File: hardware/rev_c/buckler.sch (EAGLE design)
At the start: 61 parts, among them J1 DB25_5747846, J2 DM3AT-SF-PEJM5, J3 GROVE-CONNECTOR-DIP(4P-2.0), J4 GROVE-CONNECTOR-DIP(4P-2.0), J5 GROVE-CONNECTOR-DIP(4P-2.0), J6 GROVE-CONNECTOR-DIP(4P-2.0), J7 NRF52832DK_SHIELD, U1 ADXL327, U2 MAX44009, U3 MPU-9250, U4 MS5637-02BA03, U5 SI7021-A20-GM1, U6 SIP32510

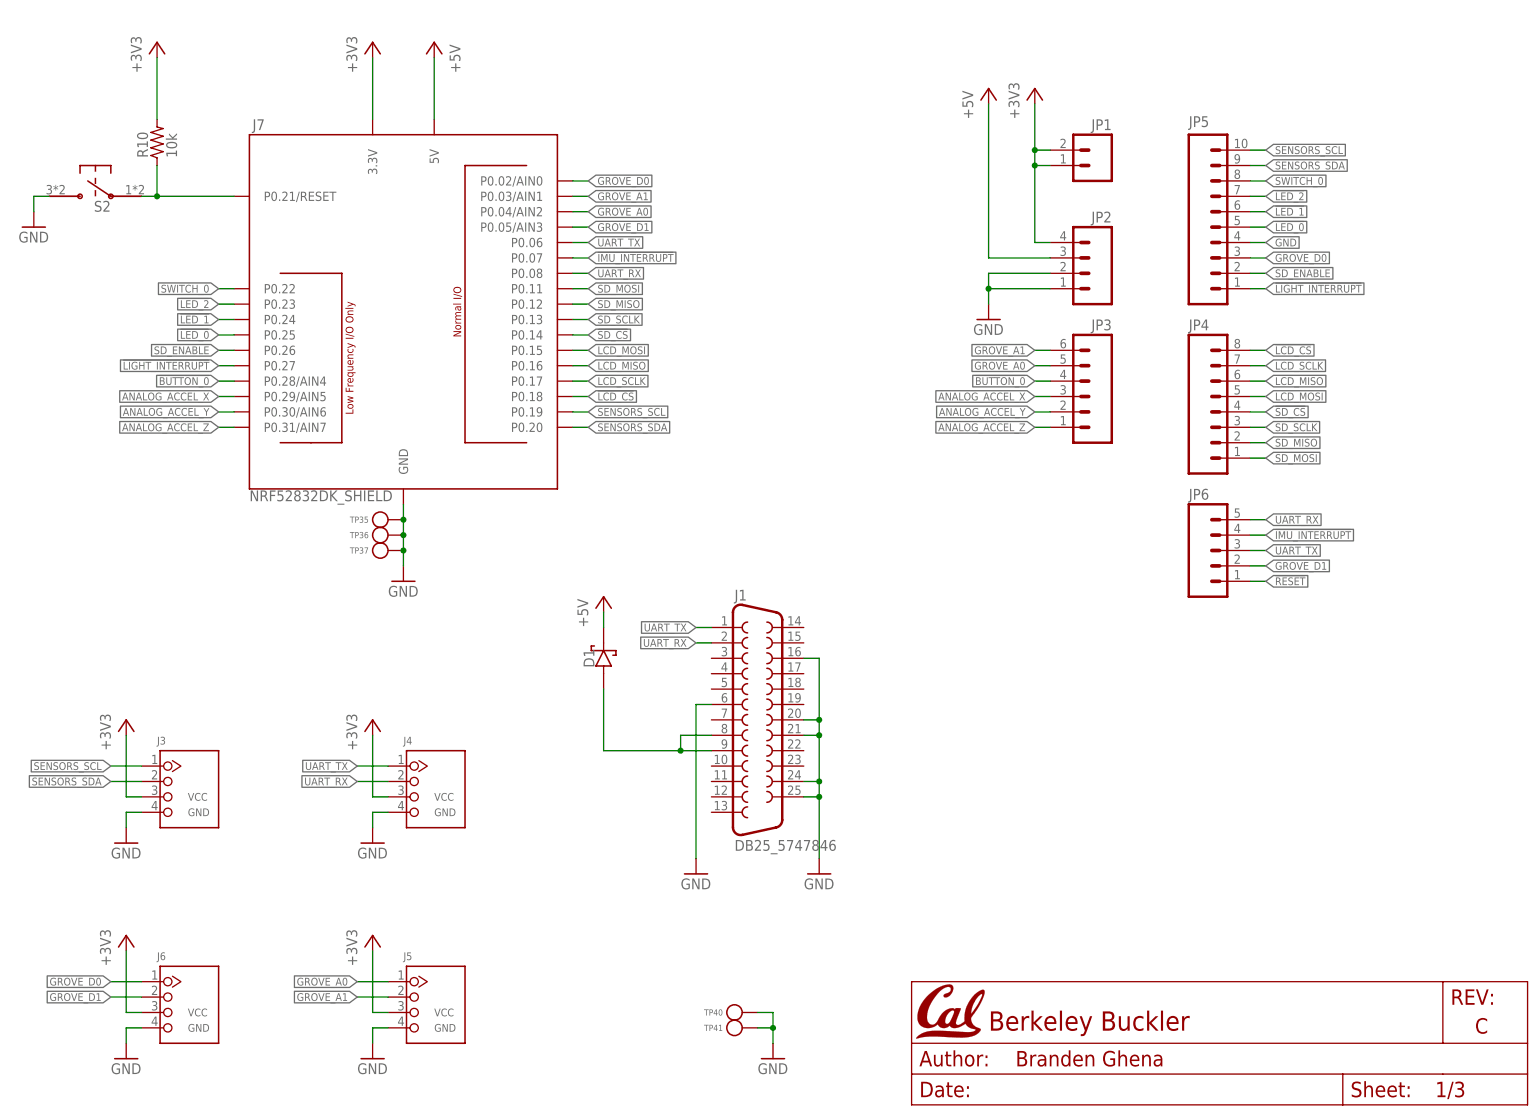
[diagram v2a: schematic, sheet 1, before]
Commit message: renumber headers
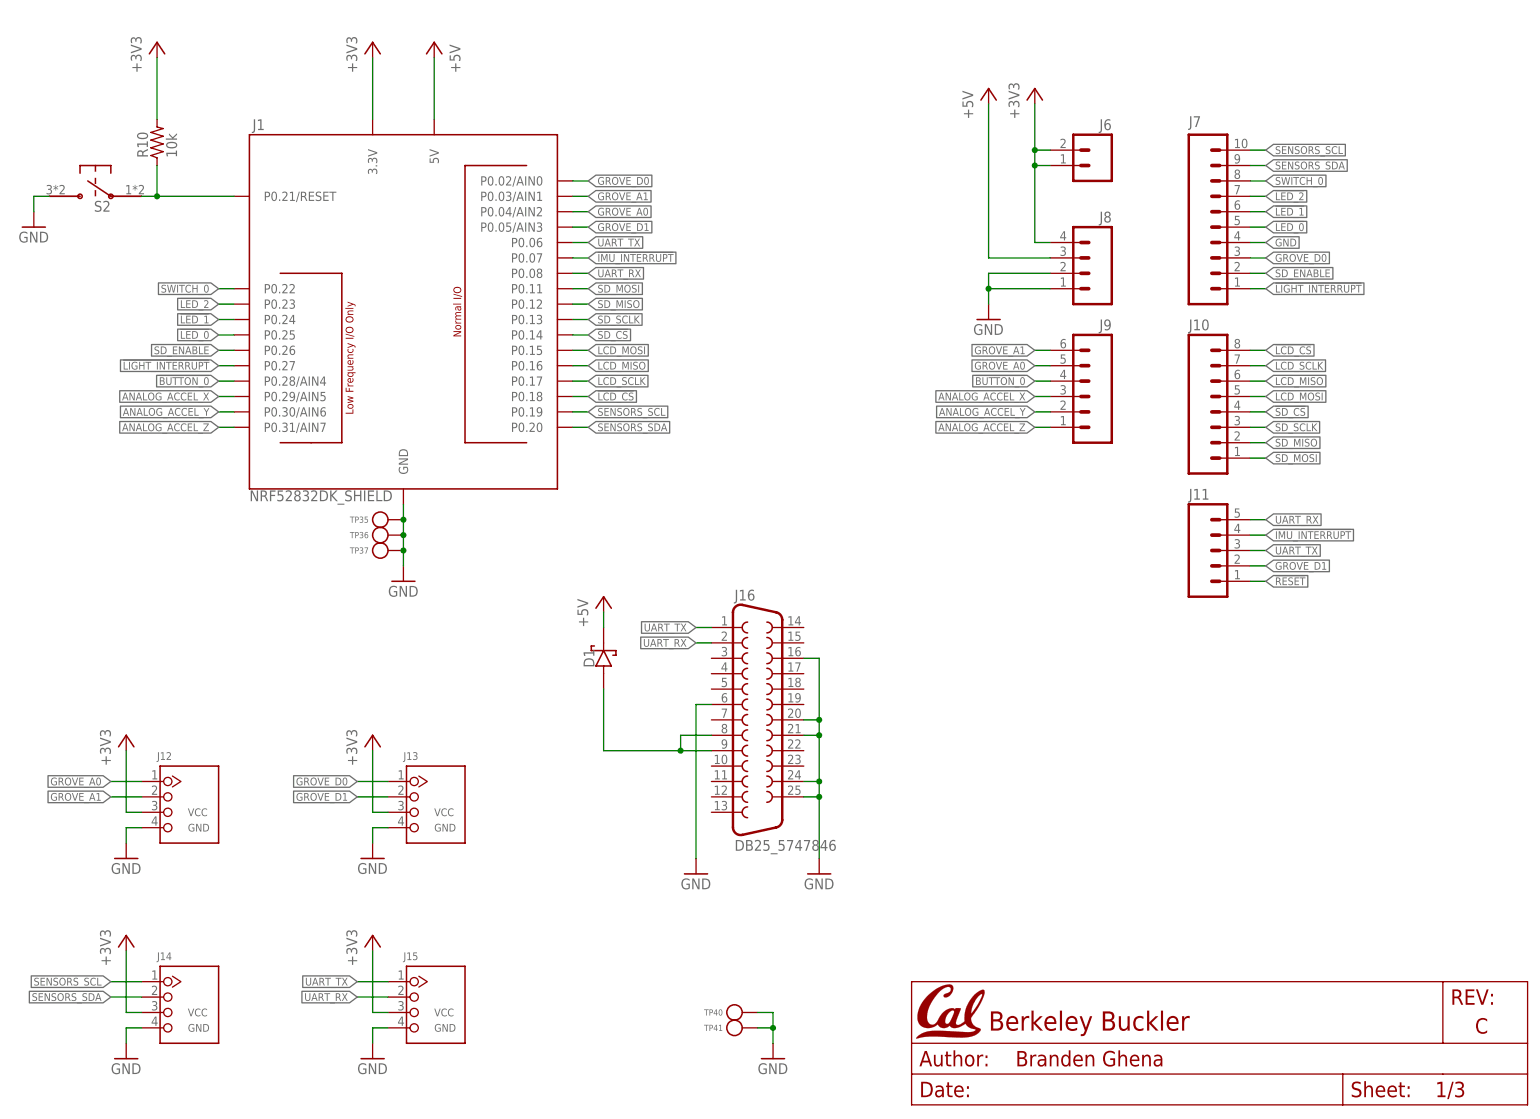
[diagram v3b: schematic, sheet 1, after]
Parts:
- removed J3, J4: GROVE-CONNECTOR-DIP(4P-2.0), headers:GROVE-CONNECTOR-DIP(4P-2.0)
- removed JP1: (no value), SparkFun-Connectors:M02PTH
- removed JP5: M10", SparkFun-Connectors:M10"
- added J12, J13, J14: GROVE-CONNECTOR-DIP(4P-2.0), headers:GROVE-CONNECTOR-DIP(4P-2.0)
- added J16: DB25_5747846, headers:DB25_5747846
- J1: value DB25_5747846 -> NRF52832DK_SHIELD; device headers:DB25_5747846 -> headers:NRF52832DK_SHIELD; DESCRIPTION CONN D-SUB RCPT 25POS R/A SOLDER -> (none); DIGIKEY1 (none) -> S1011EC-10-ND; DIGIKEY2 (none) -> S1011EC-08-ND; DIGIKEY3 (none) -> S1011EC-08-ND; DIGIKEY4 (none) -> S1011EC-06-ND; DIGIKEY5 (none) -> S1011EC-09-ND; MANUFACTURER TE Connectivity AMP Connectors -> (none); MPN 5747846-4 -> (none)
- J6: value GROVE-CONNECTOR-DIP(4P-2.0) -> (none); device headers:GROVE-CONNECTOR-DIP(4P-2.0) -> SparkFun-Connectors:M02PTH; DESCRIPTION Grove - Universal 4 pin connector -> (none); DIGIKEY (none) -> S1011EC-02-ND; MANUFACTURER Seeed Studio -> (none); MOUSER 713-110990030 -> (none); MPN 110990030 -> (none)
- J7: value NRF52832DK_SHIELD -> M10"; device headers:NRF52832DK_SHIELD -> SparkFun-Connectors:M10"; DIGIKEY (none) -> S1011EC-10-ND; DIGIKEY1 S1011EC-10-ND -> (none); DIGIKEY2 S1011EC-08-ND -> (none); DIGIKEY3 S1011EC-08-ND -> (none); DIGIKEY4 S1011EC-06-ND -> (none); DIGIKEY5 S1011EC-09-ND -> (none)
- renumbered J2 to J17, J5 to J15, JP2 to J8, JP3 to J9, JP4 to J10, JP6 to J11
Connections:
- net !BUTTON_0: now also J1.P0.28/AIN4; no longer J7.P0.28/AIN4
- net !IMU_INTERRUPT: now also J1.P0.07; no longer J7.P0.07
- net !LCD_CS: now also J1.P0.18; no longer J7.P0.18
- net !LED_0: now also J1.P0.25, J7.5; no longer J7.P0.25, JP5.5
- net !LED_1: now also J1.P0.24, J7.6; no longer J7.P0.24, JP5.6
- net !LED_2: now also J1.P0.23, J7.7; no longer J7.P0.23, JP5.7
- net !LIGHT_INTERRUPT: now also J1.P0.27, J7.1; no longer J7.P0.27, JP5.1
- net !RESET: now also J1.P0.21/RESET; no longer J7.P0.21/RESET
- net !SD_CS: now also J1.P0.14; no longer J7.P0.14
- net +3V3: now also J1.3.3V, J12.3, J13.3, J14.3, J6.1, J6.2; no longer J3.3, J4.3, J6.3, J7.3.3V, JP1.1, JP1.2
- net +5V: now also J1.5V; no longer J7.5V
- net 5V_IN: now also J16.8, J16.9; no longer J1.8, J1.9
- net ANALOG_ACCEL_X: now also J1.P0.29/AIN5; no longer J7.P0.29/AIN5
- net ANALOG_ACCEL_Y: now also J1.P0.30/AIN6; no longer J7.P0.30/AIN6
- net ANALOG_ACCEL_Z: now also J1.P0.31/AIN7; no longer J7.P0.31/AIN7
- net GND: now also J1.GND, J12.4, J13.4, J14.4, J16.16, J16.20, J16.21, J16.24, J16.25, J16.6, J7.4; no longer J1.16, J1.20, J1.21, J1.24, J1.25, J1.6, J3.4, J4.4, J6.4, J7.GND, JP5.4
- net GROVE_A0: now also J1.P0.04/AIN2, J12.1; no longer J15.1, J7.P0.04/AIN2
- net GROVE_A1: now also J1.P0.03/AIN1, J12.2; no longer J15.2, J7.P0.03/AIN1
- net GROVE_D0: now also J1.P0.02/AIN0, J13.1, J7.3; no longer J6.1, J7.P0.02/AIN0, JP5.3
- net GROVE_D1: now also J1.P0.05/AIN3, J13.2; no longer J6.2, J7.P0.05/AIN3
- net LCD_MISO: now also J1.P0.16; no longer J7.P0.16
- net LCD_MOSI: now also J1.P0.15; no longer J7.P0.15
- net LCD_SCLK: now also J1.P0.17; no longer J7.P0.17
- net SD_ENABLE: now also J1.P0.26, J7.2; no longer J7.P0.26, JP5.2
- net SD_MISO: now also J1.P0.12; no longer J7.P0.12
- net SD_MOSI: now also J1.P0.11; no longer J7.P0.11
- net SD_SCLK: now also J1.P0.13; no longer J7.P0.13
- net SENSORS_SCL: now also J1.P0.19, J14.1, J7.10; no longer J3.1, J7.P0.19, JP5.10
- net SENSORS_SDA: now also J1.P0.20, J14.2, J7.9; no longer J3.2, J7.P0.20, JP5.9
- net SWITCH_0: now also J1.P0.22, J7.8; no longer J7.P0.22, JP5.8
- net UART_RX: now also J1.P0.08, J15.2, J16.2; no longer J1.2, J4.2, J7.P0.08
- net UART_TX: now also J1.P0.06, J15.1, J16.1; no longer J1.1, J4.1, J7.P0.06

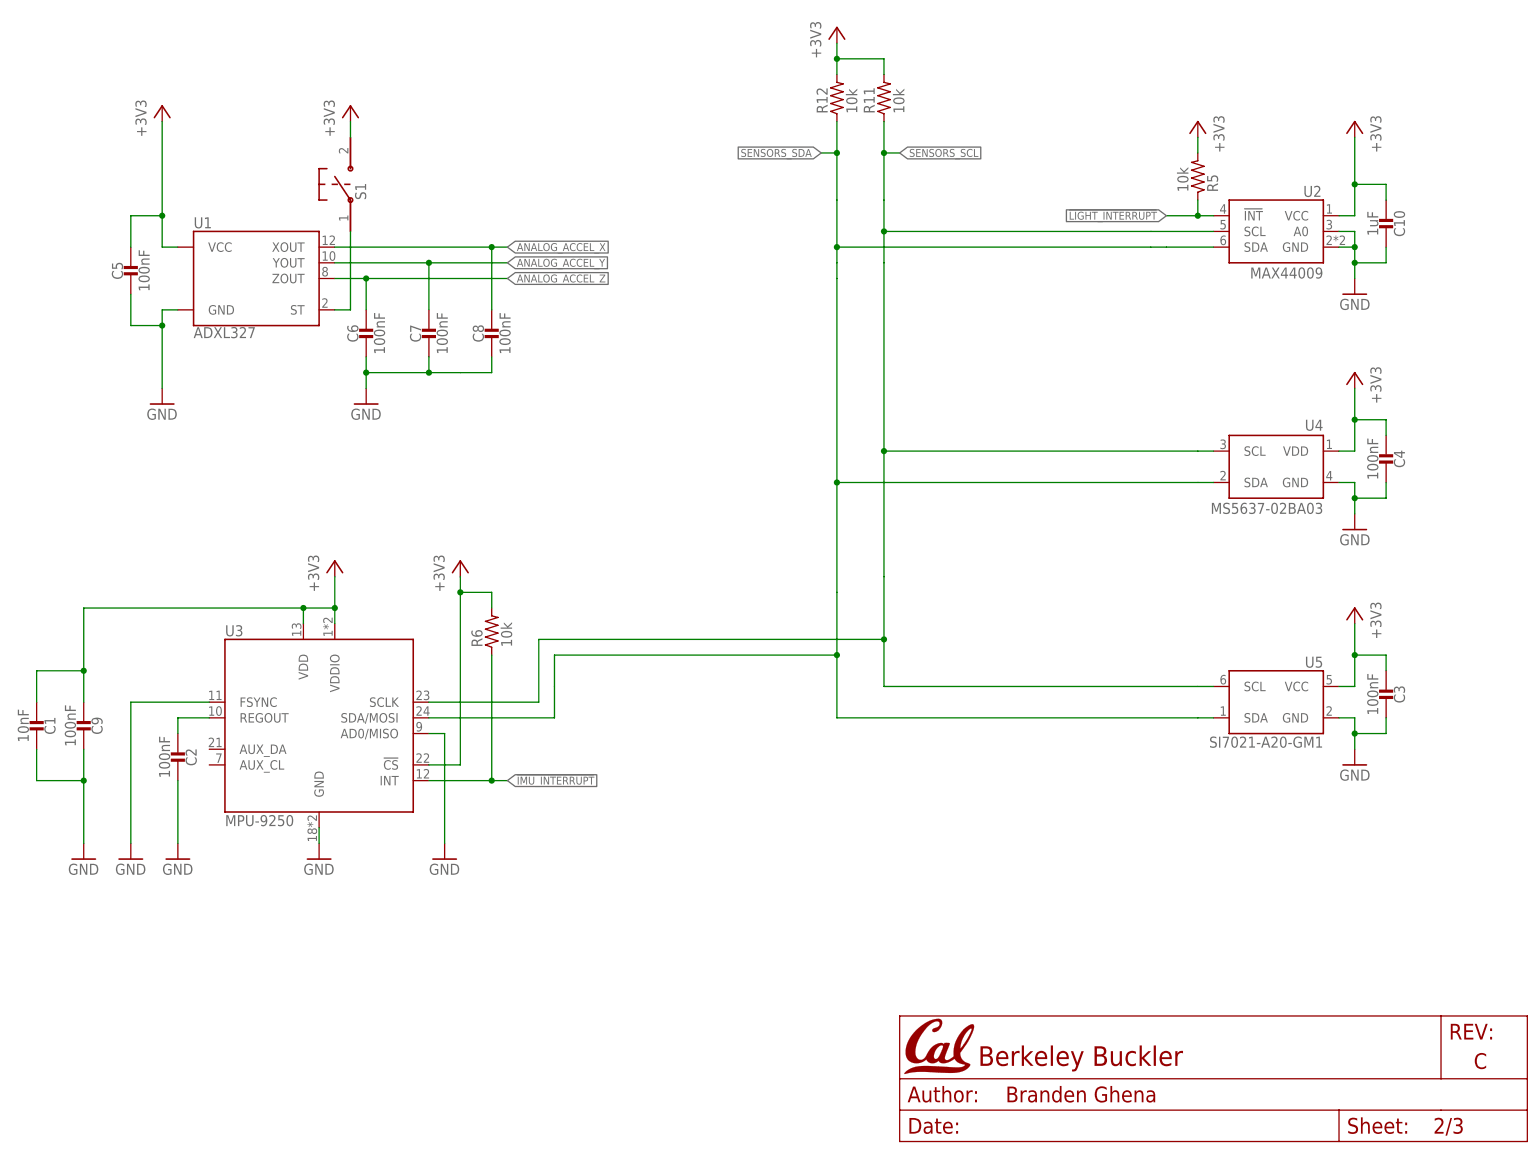
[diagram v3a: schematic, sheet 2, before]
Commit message: replace digital acc with lsm9ds1tr
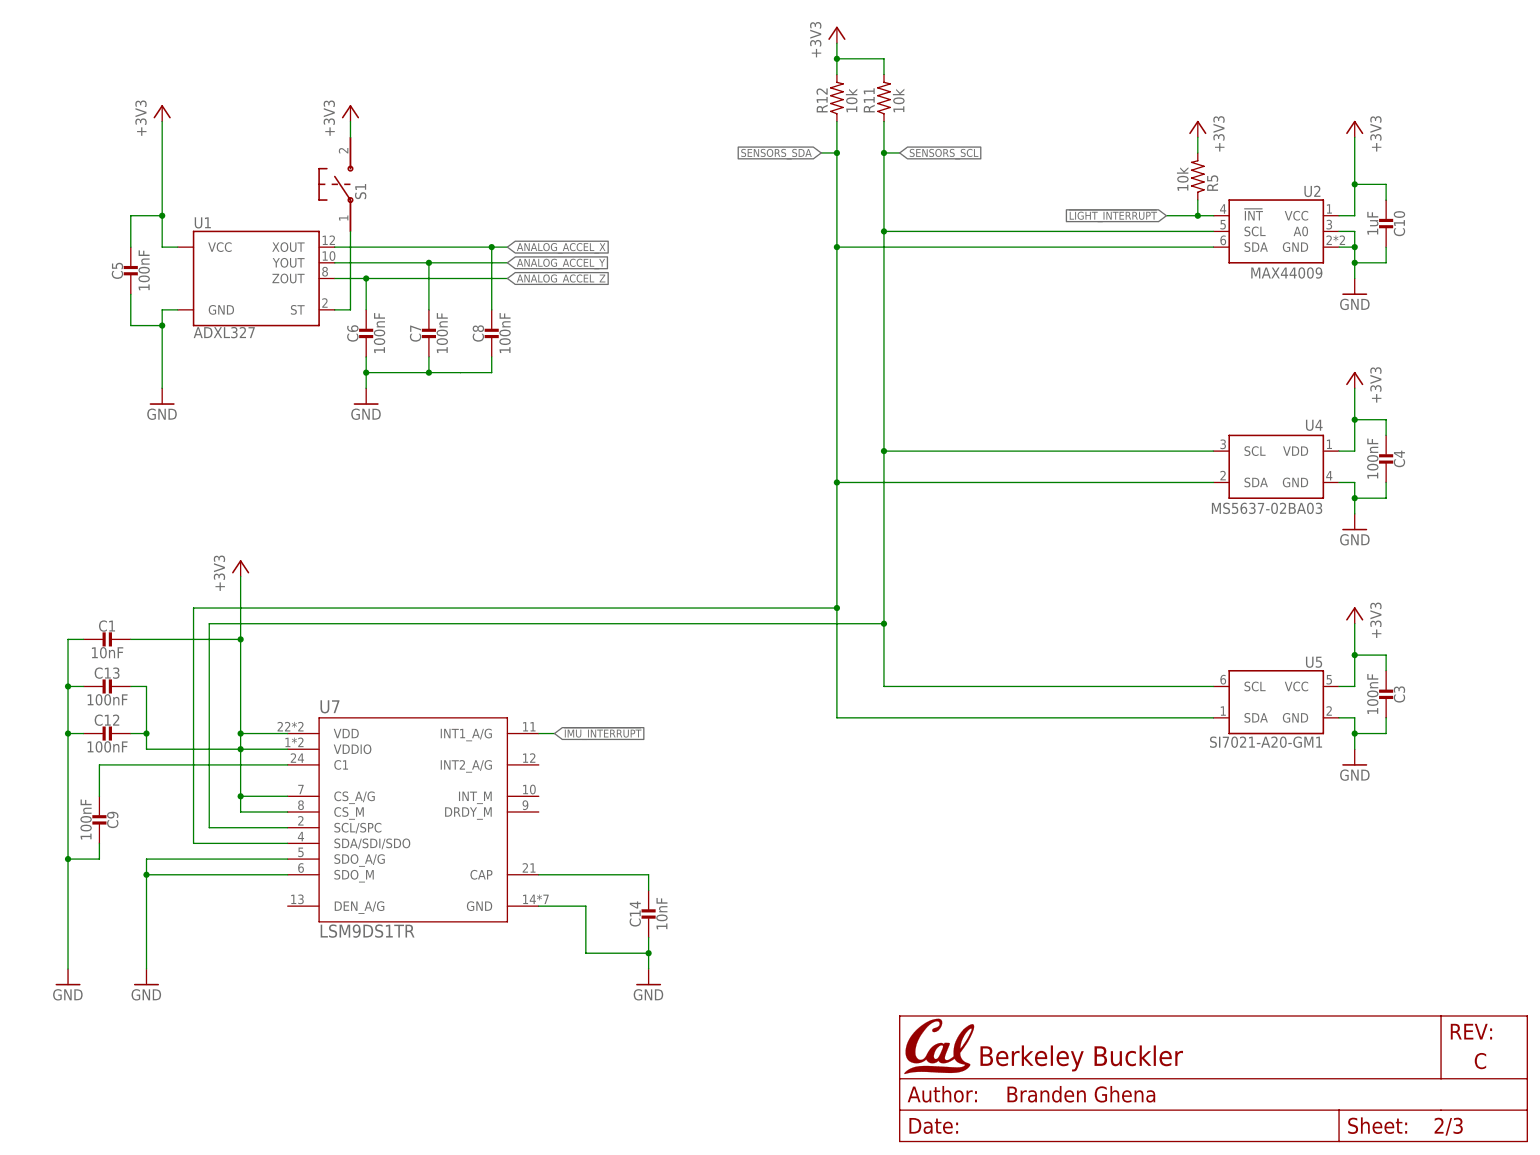
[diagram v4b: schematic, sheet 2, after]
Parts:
- removed C2: 100nF, passives:CAPACITOR0402_CAP
- removed R6: 10k, passives:RESISTOR0402_RES
- removed U3: MPU-9250, chips:MPU-9250
- added C12, C13: 100nF, passives:CAPACITOR0402_CAP
- added C14: 10nF, passives:CAPACITOR0402_CAP
- added U7: LSM9DS1TR, chips:LSM9DS1TR
- renumbered A1 to J18
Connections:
- removed net N$19: C2.1, U3.REGOUT
- new net N$1: C9.1, U7.C1
- new net N$6: C14.2, U7.CAP
- net !IMU_INTERRUPT: now also U7.INT1_A/G; no longer R6.1, U3.INT
- net +3V3: now also C1.2, C12.2, C13.2, U7.CS_A/G, U7.CS_M, U7.VDD, U7.VDDIO; no longer C1.1, C9.1, R6.2, U3.!CS, U3.VDD, U3.VDDIO
- net GND: now also C1.1, C12.1, C13.1, C14.1, U7.GND, U7.SDO_A/G, U7.SDO_M; no longer C1.2, C2.2, U3.AD0/MISO, U3.FSYNC, U3.GND
- net SENSORS_SCL: now also U7.SCL/SPC; no longer U3.SCLK
- net SENSORS_SDA: now also U7.SDA/SDI/SDO; no longer U3.SDA/MOSI
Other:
- note added: "AG I2C Address: 0x6A M I2C Address: 0x1C"
- note removed: "I2C Address: 0x68"
- moved on the sheet: C1, C9
